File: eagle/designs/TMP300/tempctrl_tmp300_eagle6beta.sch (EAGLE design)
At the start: 21 parts, among them IC1 TMP300, Q1 NIF5002

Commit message: Added jumper instance.
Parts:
- added SJ1: (no value), jumper:SJ
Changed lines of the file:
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@@
 <part name="P+4" library="supply1" deviceset="+12V" device=""/>
 <part name="VSS" library="wirepad" deviceset="2,54/1,0" device="" value="GND"/>
+<part name="SJ1" library="jumper" deviceset="SJ" device=""/>
 </parts>
 <sheets>
@@
 <instance part="P+4" gate="1" x="106.68" y="154.94"/>
 <instance part="VSS" gate="P" x="104.14" y="175.26" rot="R270"/>
+<instance part="SJ1" gate="1" x="53.34" y="88.9"/>
 </instances>
 <busses>

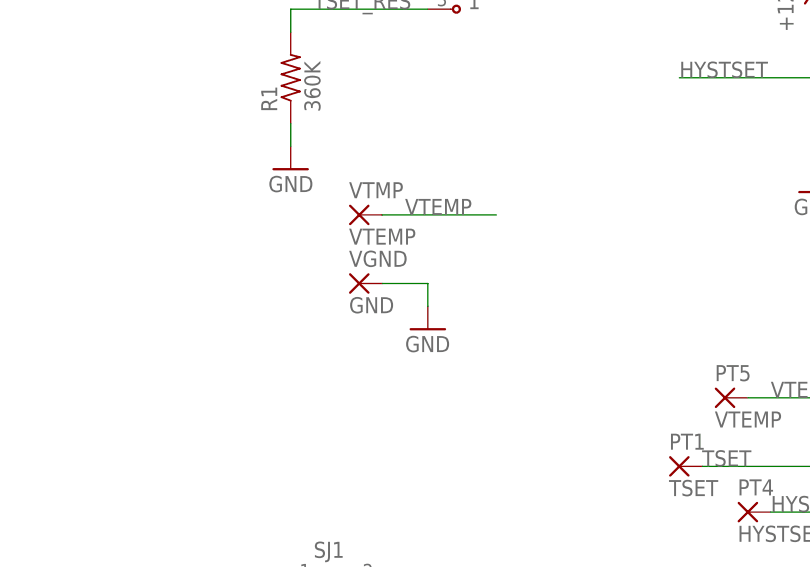
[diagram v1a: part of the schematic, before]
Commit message: Deleted wire segment.
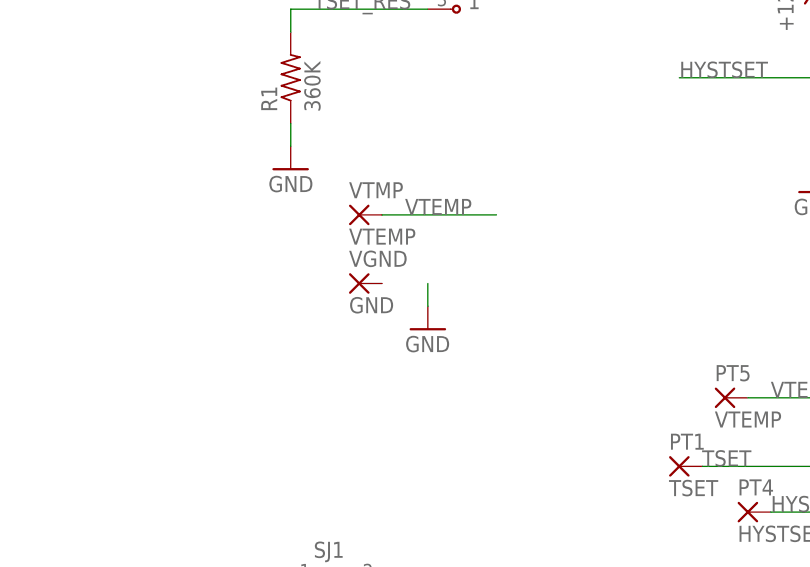
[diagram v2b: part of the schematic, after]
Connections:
- net GND: no longer VGND.P
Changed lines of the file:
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@@
 </segment>
 <segment>
-<wire x1="58.42" y1="121.92" x2="63.5" y2="121.92" width="0.1524" layer="91"/>
 <wire x1="63.5" y1="121.92" x2="63.5" y2="119.38" width="0.1524" layer="91"/>
-<pinref part="VGND" gate="P" pin="P"/>
 <pinref part="GND7" gate="1" pin="GND"/>
 </segment>
